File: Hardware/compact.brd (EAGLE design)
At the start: 30.5 x 44.5 mm, 24 parts, among them SW1 SWITCH_SPDT, U1 MCP73831, U2 EDISON_CONNECTOR_FULLMOUNTING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, U3 EDISON_CONNECTOR_FULLHEADER

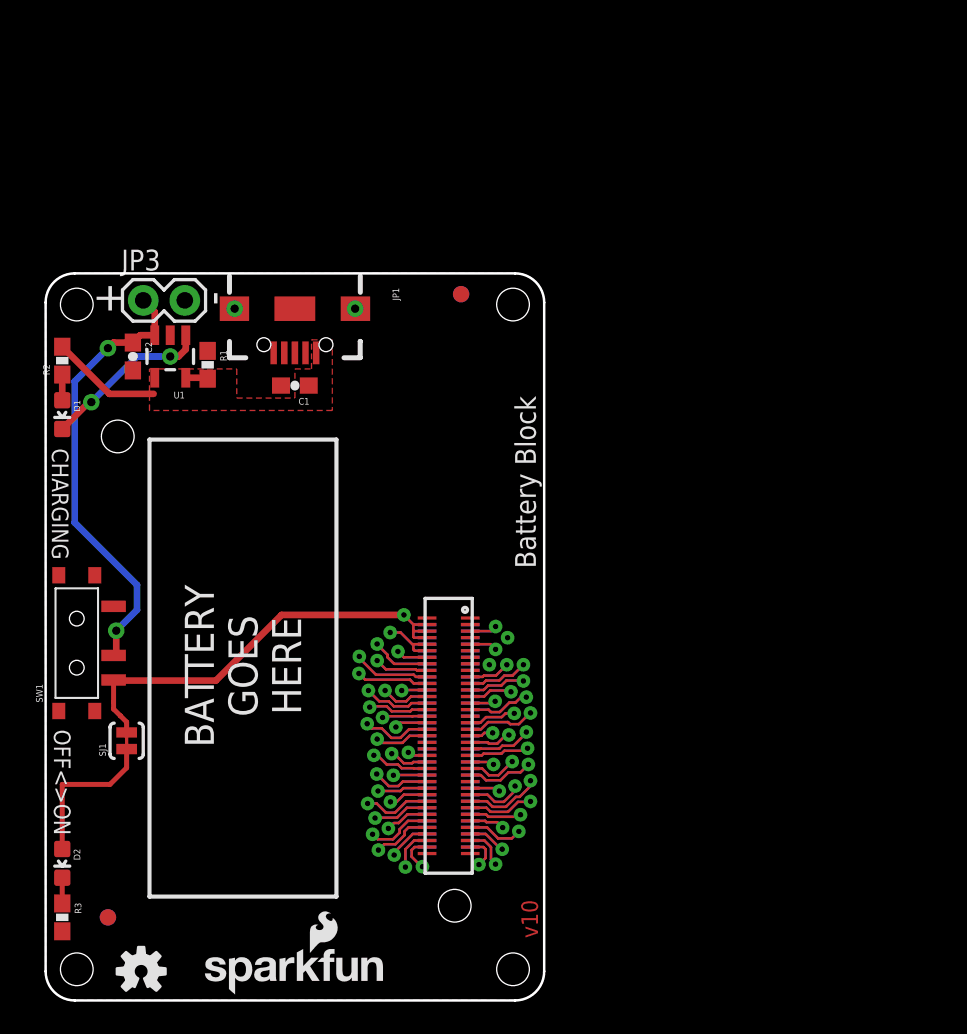
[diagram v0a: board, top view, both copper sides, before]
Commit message: Initial HP95LX daughterboard layouts
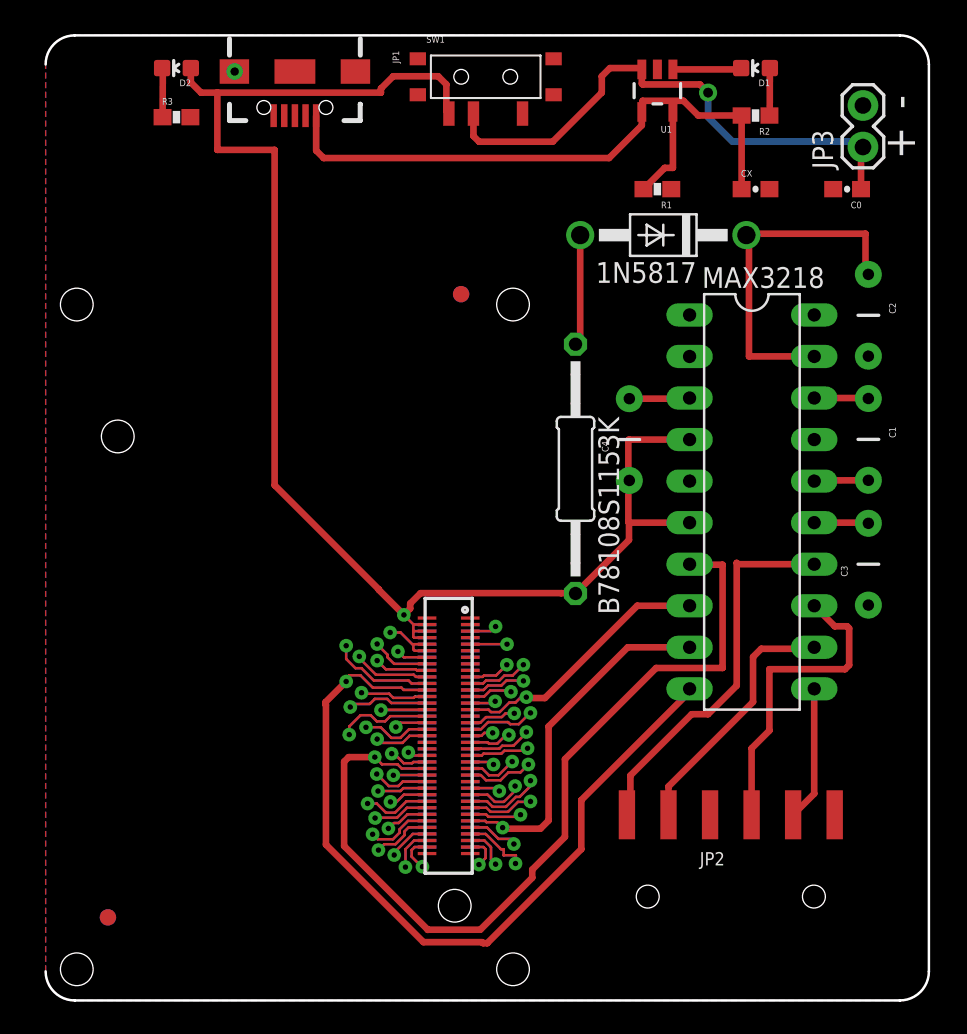
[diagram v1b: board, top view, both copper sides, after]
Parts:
- removed FRAME1: FRAME-LETTER, SparkFun-Aesthetics:CREATIVE_COMMONS
- removed LOGO1, LOGO2: OSHW-LOGOS, SparkFun-Aesthetics:OSHW-LOGO-S
- removed LOGO3, LOGO4: SFE_LOGO_NAME_FLAME.1_INCH, SparkFun-Aesthetics:SFE_LOGO_NAME_FLAME_.1
- removed SJ1: LED DISABLE, SparkFun-Passives:PAD-JUMPER-2-NC_BY_TRACE_YES_SILK
- added 1N5817: (no value), diode:DO41-10
- added B78108S1153K: 15uH, resistor:0207/15
- added C0, CX: 4.7uF, SparkFun-Capacitors:0603-CAP
- added C3, C4: 1uF, SparkFun-Capacitors:CAP-PTH-5MM
- added JP2: RA 6Pin SMD, SparkFun-Connectors:1X06-SMD
- added MAX3218: (no value), ic-package:DIL20
- C1: value 4.7uF -> 0.47uF; device SparkFun-Capacitors:0603-CAP -> SparkFun-Capacitors:CAP-PTH-5MM
- C2: value 4.7uF -> 1uF; device SparkFun-Capacitors:0603-CAP -> SparkFun-Capacitors:CAP-PTH-5MM
- moved FRAME2 65.1 mm to (49.5, -54.6)
- moved R3 49.4 mm to (8.00, 54.0), turned to 0 degrees
- moved D2 49.1 mm to (8.00, 57.0), turned to 90 degrees
- moved D1 47.4 mm to (43.4, 57.0), turned to 90 degrees
- moved C2 45.0 mm to (50.3, 41.9)
- moved JP3 45.0 mm to (50.0, 52.2), turned to 90 degrees
- moved R2 45.0 mm to (43.4, 54.1), turned to 180 degrees
- moved SW1 42.7 mm to (26.9, 56.5), turned to 180 degrees
- moved C1 35.2 mm to (50.3, 34.3), turned to 270 degrees
- moved U1 33.9 mm to (37.4, 55.6)
- moved R1 29.5 mm to (37.4, 49.6), turned to 180 degrees
- moved JP1 14.5 mm to (15.2, 56.8)
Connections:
- removed net N$7: D2.A, SJ1.1
- removed net VIN: C1.1, JP1.VBUS1, R2.2, U1.4
- new net 1: 1N5817.A, B78108S1153K.1, MAX3218.1
- new net CX: CX.1, JP1.VBUS1, R2.2, U1.4
- new net N$10: JP2.4, MAX3218.13
- new net N$11: JP2.2, MAX3218.12
- new net N$13: JP2.5, MAX3218.11
- new net N$14: 1N5817.C, C2.1, MAX3218.19
- new net N$6: C3.2, MAX3218.15
- new net N$8: C1.1, MAX3218.18
- new net N$9: C1.2, MAX3218.16
- new net T1OUT: JP2.1, MAX3218.14
- net GND: now also C0.2, C3.1, C4.2, CX.2, JP2.3, JP2.6, MAX3218.17, MAX3218.20, MAX3218.3, MAX3218.5; no longer C1.2
- net GP130_UART_1_RX: now also MAX3218.9
- net GP131_UART_1_TX: now also MAX3218.7
- net GP134_UART_2_RX: now also MAX3218.10
- net GP135_UART_2_TX: now also MAX3218.8
- net VBAT: now also C0.1; no longer C2.1
- net VSYS: now also B78108S1153K.2, C4.1, D2.A, MAX3218.4, MAX3218.6; no longer SJ1.2
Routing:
- net VSYS: track 31.3 -> 96.0 mm
- net GP134_UART_2_RX: track 3.13 -> 55.2 mm
- net GP131_UART_1_TX: track 7.18 -> 57.4 mm
- net CX: track 0.00 -> 35.5 mm
- net T1OUT: track 0.00 -> 23.5 mm
- net N$14: track 0.00 -> 21.6 mm
- net GP130_UART_1_RX: track 4.30 -> 23.9 mm
- net N$10: track 0.00 -> 19.3 mm
- net N$11: track 0.00 -> 15.8 mm
- net GP135_UART_2_TX: track 7.74 -> 20.1 mm
- net N$7: track 9.45 -> 0.00 mm
- net N$13: track 0.00 -> 8.23 mm
- net 1: track 0.00 -> 6.96 mm
- net VIN: track 6.78 -> 0.00 mm
- net VBAT: track 27.4 -> 33.8 mm, vias 2 -> 1
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- removed copper zone on layer 1, net VIN
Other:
- board size 30.5 x 44.5 mm -> 54 x 59 mm
- board text added: "Ben Lamb"
- board text removed: "4xM2.0"
- board text removed: "BATTERY GOES HERE"
- board text removed: "Battery Block"
- board text removed: "CHARGING"
- board text removed: "OFF<>ON"
- board text removed: "v10"
